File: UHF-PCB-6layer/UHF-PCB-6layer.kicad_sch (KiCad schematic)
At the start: 14 parts, among them U1 MAC-24+, U2 MC100EPT22D, U3 TAV1-331+, U4 TPS3103K33DBVR, U5 XMSM0G3507SPT, U6 XC7A100T-CSG324_A

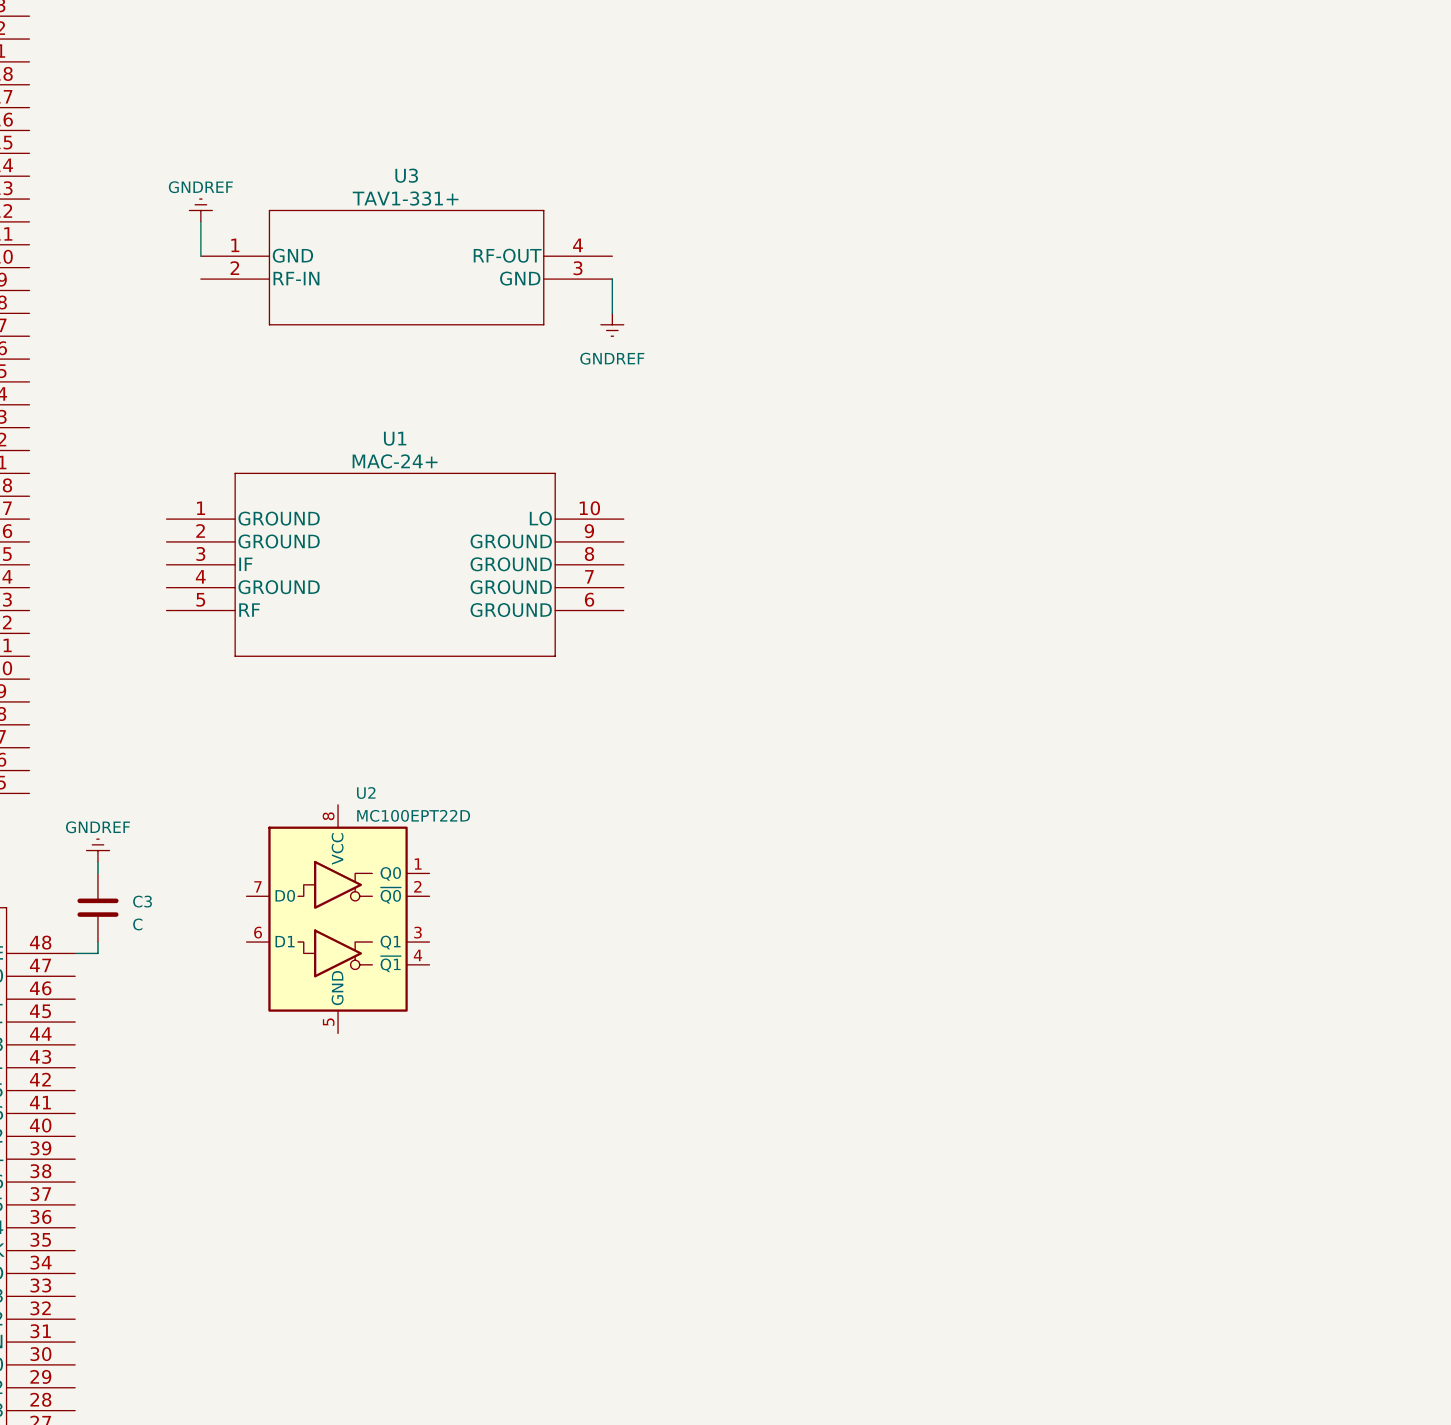
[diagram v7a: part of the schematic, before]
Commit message: VCO changed to right module, still need to connect stuff and addd caps + resis + induct
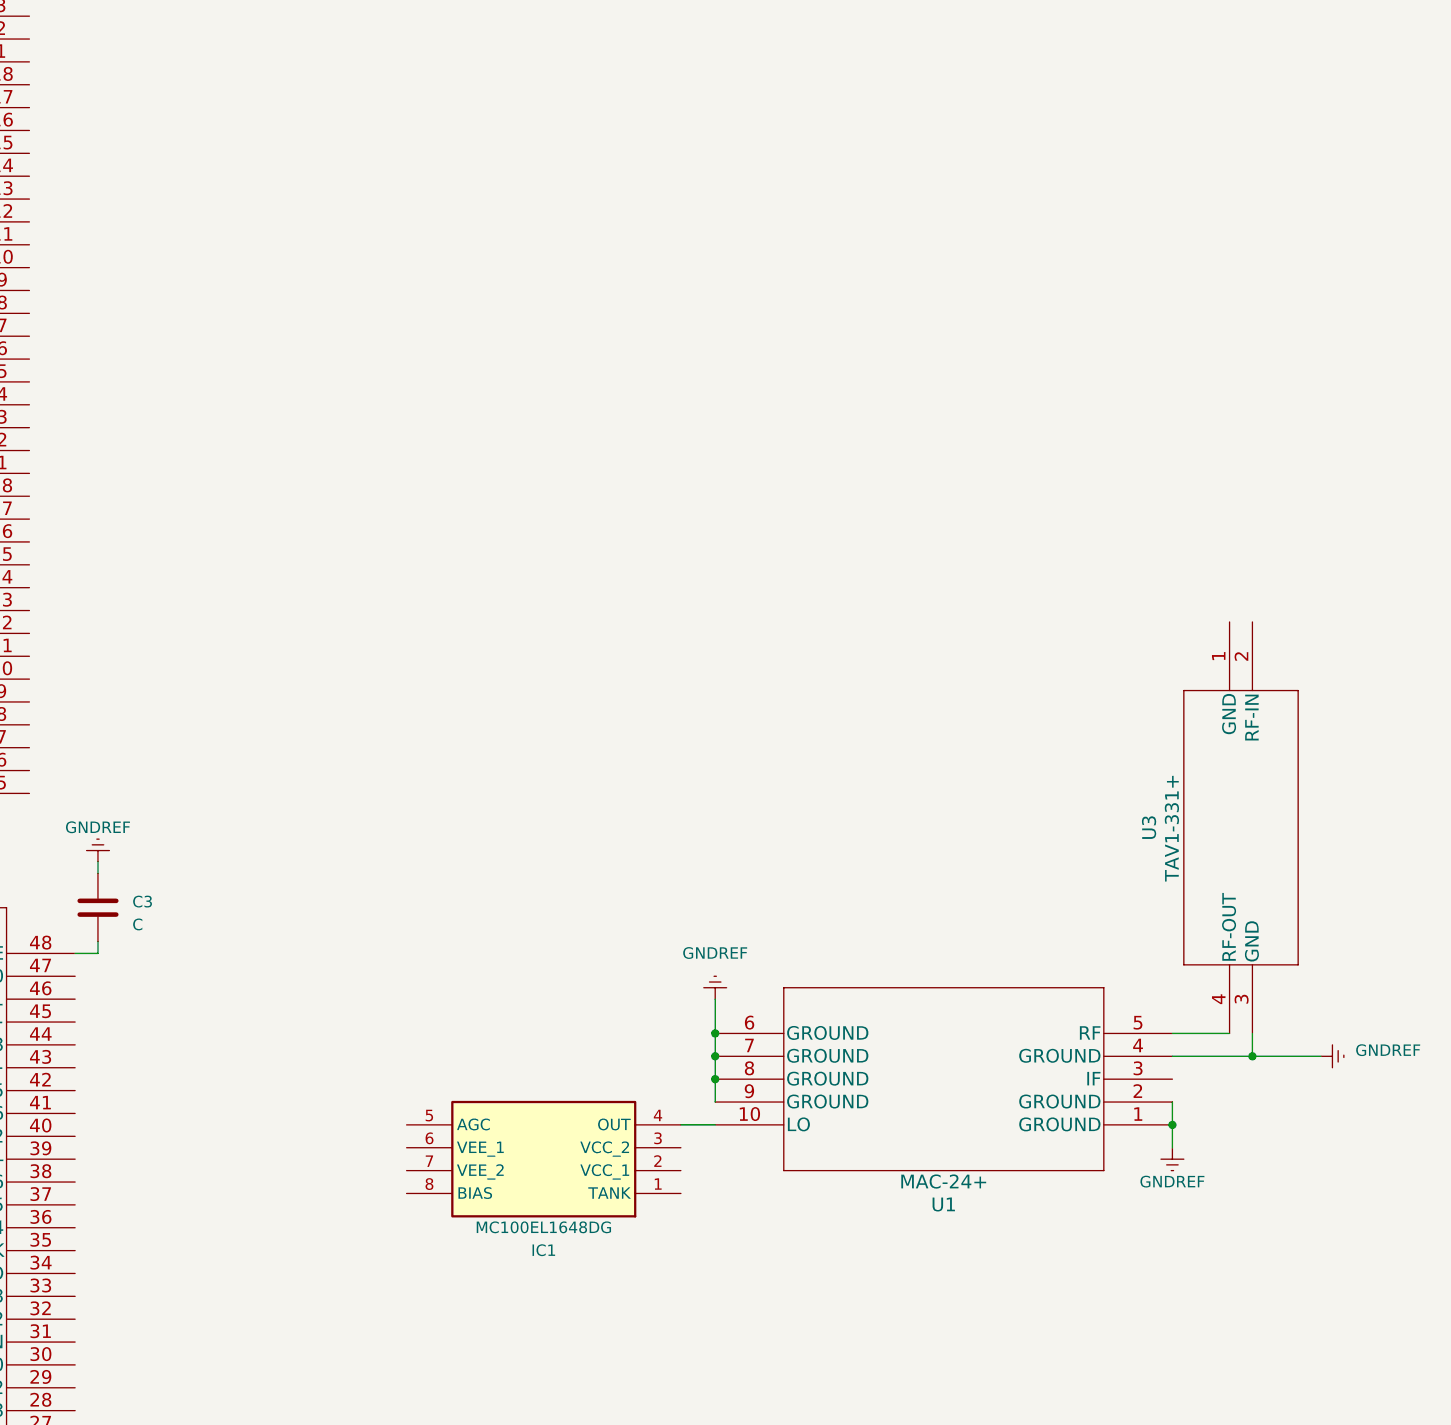
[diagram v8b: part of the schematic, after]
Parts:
- removed U2: MC100EPT22D, Package_SO:SOIC-8_3.9x4.9mm_P1.27mm, symbol Interface:MC100EPT22D
- added IC1: MC100EL1648DG, SOIC127P600X175-8N, symbol MC100EL1648DG:MC100EL1648DG
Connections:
- net GNDREF: now also U1.1 (GROUND), U1.2 (GROUND), U1.4 (GROUND), U1.6 (GROUND), U1.7 (GROUND), U1.8 (GROUND), U1.9 (GROUND); no longer U3.1 (GND)
- net at U1.10 (LO): now also IC1.4 (OUT)
- net at U1.5 (RF): now also U3.4 (RF-OUT)
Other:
- moved on the sheet: U1, U3
